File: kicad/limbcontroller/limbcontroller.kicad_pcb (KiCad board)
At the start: 2 copper layers, 51.5 x 44 mm, 38 parts, among them J3 Screw_Terminal_01x05, J4 Screw_Terminal_01x05, J5 USB_C_Receptacle_USB2.0_14P, M1 Stepper_Motor_bipolar, Q1 DTB143EK, SW2 1825910-6, SW3 1825910-6, U1 RT9193-33GB, U5 STM32F103C8T6, U6 BMI323

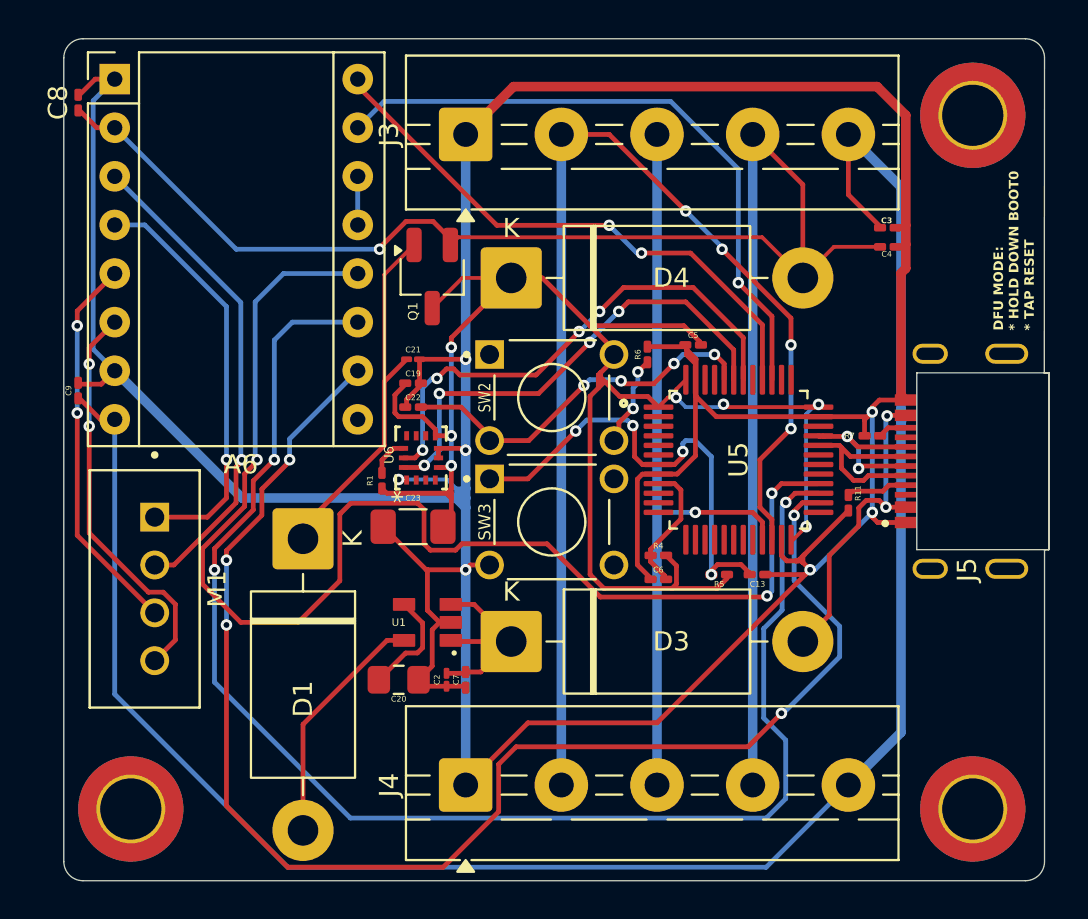
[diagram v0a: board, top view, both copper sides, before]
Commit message: cleaned up kicad files and changed 1uf capacitors to 0805 SMD size
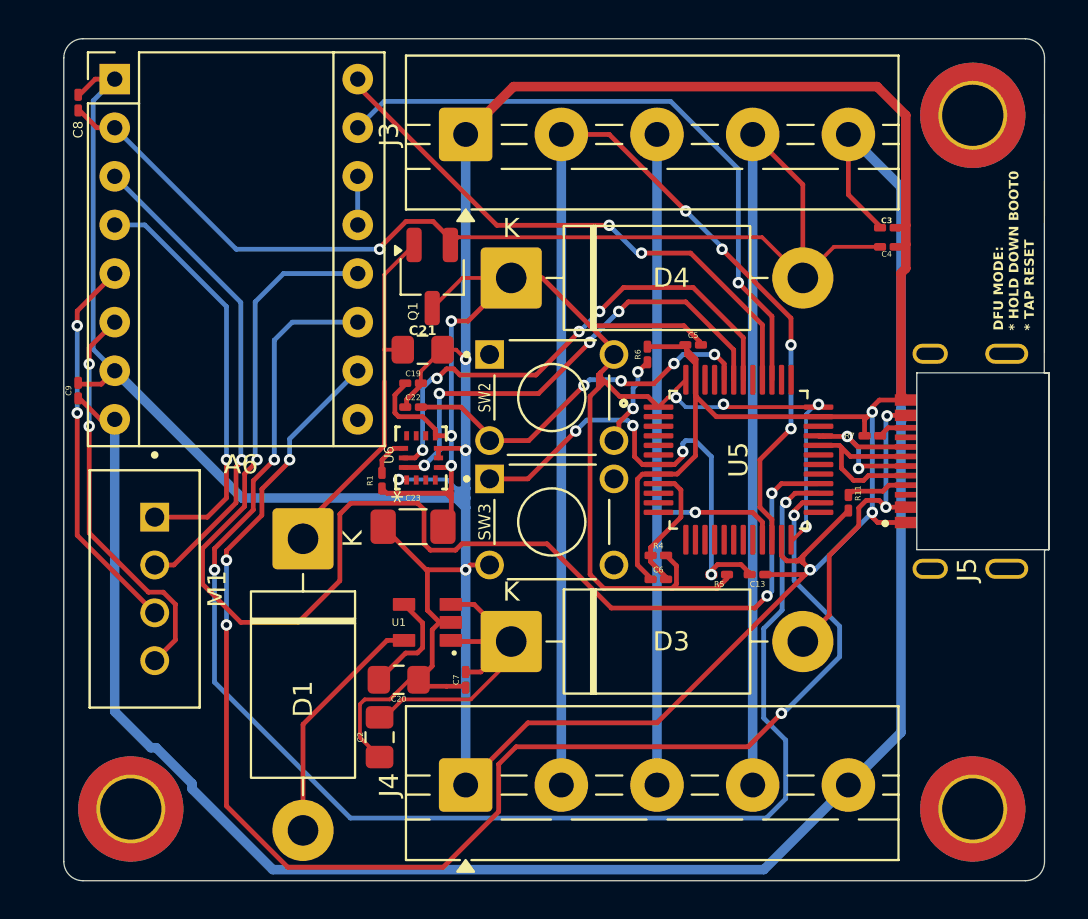
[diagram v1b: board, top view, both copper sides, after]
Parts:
- C2, C21: footprint Capacitor_SMD:C_01005_0402Metric_Pad0.57x0.30mm_HandSolder -> Capacitor_SMD:C_0805_2012Metric_Pad1.18x1.45mm_HandSolder
- moved C2 4.61 mm to (127.5, 124.5)
- moved C21 0.71 mm to (129.8, 104.2)
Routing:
- net Net-(D3-K): track 11.2 -> 19.4 mm
- net GND: track 223.8 -> 230.6 mm
- net /VMOT: track 102.5 -> 103.3 mm
- net Net-(D1-K): track 19.4 -> 18.7 mm
- net +3.3V: track 88.1 -> 88.7 mm
